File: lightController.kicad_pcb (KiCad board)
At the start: 2 copper layers, 91.4 x 87.6 mm, 66 parts, among them J1 VIN, J2 LED STRIP, J3 ICSP, J4 DEBUG, SW1 LIGHT_ON, SW2 SECT_0_ON, SW3 BRIGHT+, SW4 SECT_1_ON, SW5 BRIGHT-, SW6 SECT_2_ON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

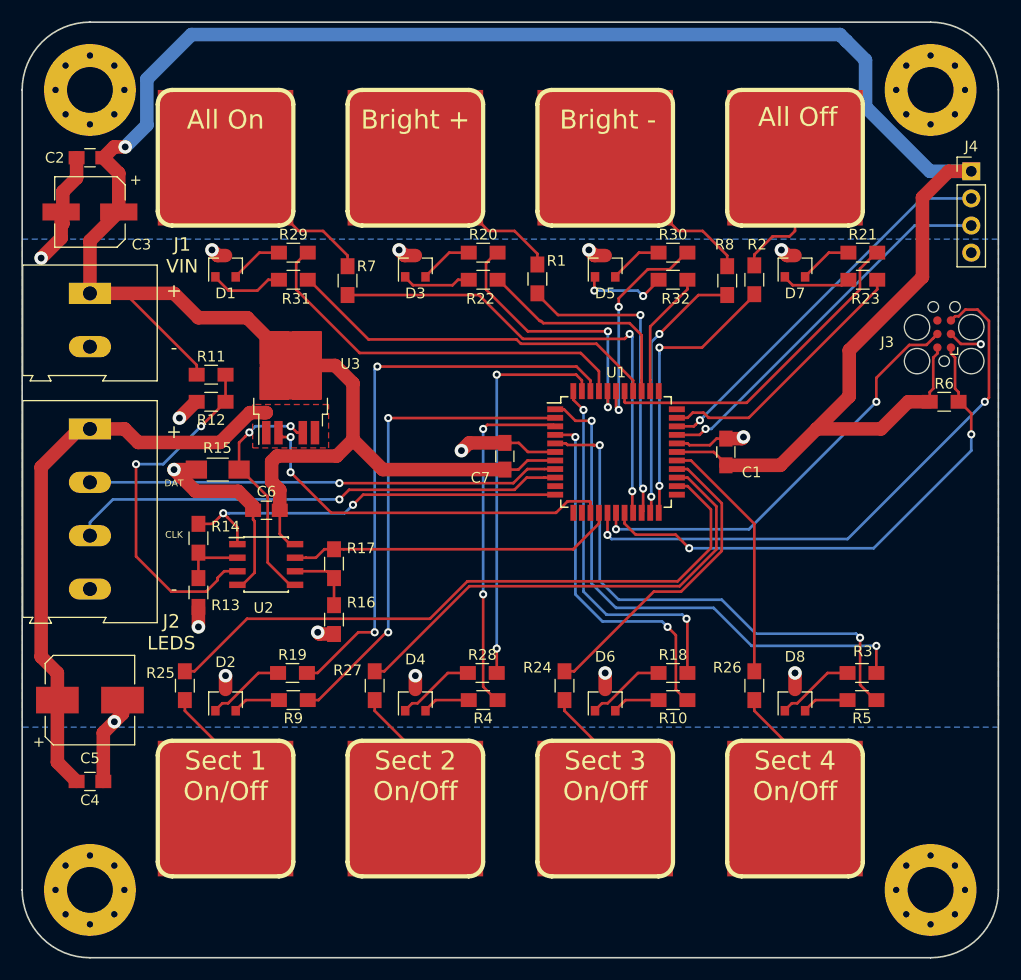
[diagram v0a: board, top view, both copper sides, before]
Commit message: Changed TX/RX to PORTB and I_SNS and PWR_EN accordingly Added SPI termination resistor footprints Added J5 GND pads
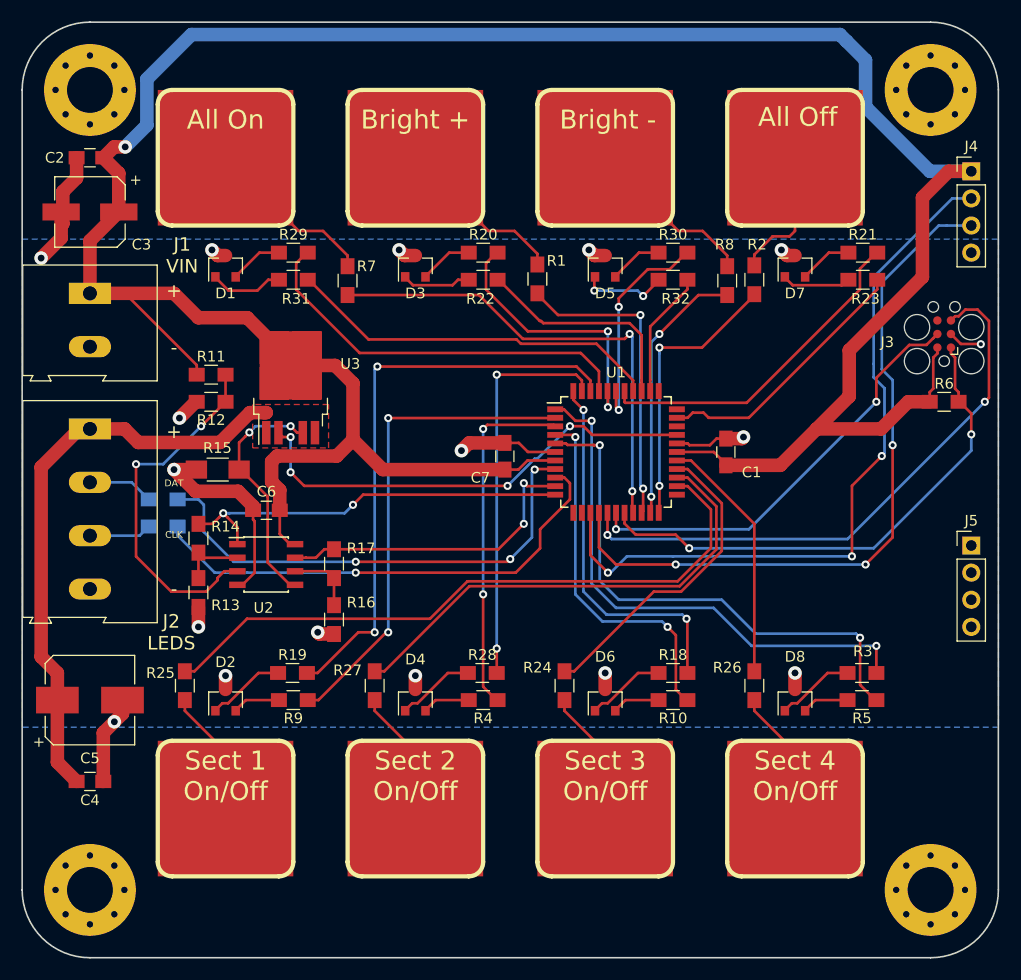
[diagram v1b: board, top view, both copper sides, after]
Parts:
- added J5: GND, Pin_Headers:Pin_Header_Straight_1x04_Pitch2.54mm, F.Cu at (174.0, 104.9)
- added R33: 1k, Resistors_SMD:R_0805_HandSoldering, B.Cu at (98.3, 103.1)
- added R34: 1k, Resistors_SMD:R_0805_HandSoldering, B.Cu at (98.3, 100.6)
- R15: value 1 -> 1k
- R17: value 4.99M -> 4.02k
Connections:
- H1 pad 1: (no net) -> Net-(H1-Pad1)
- H2 pad 1: (no net) -> Net-(H2-Pad1)
- H3 pad 1: (no net) -> Net-(H3-Pad1)
- H4 pad 1: (no net) -> Net-(H4-Pad1)
- J2 pad 2: /LED_DAT -> Net-(J2-Pad2)
- J2 pad 3: /LED_CLK -> Net-(J2-Pad3)
- J3 pad 6: (no net) -> Net-(J3-Pad6)
- U1 pad 10: (no net) -> /I_SNS
- U1 pad 12: (no net) -> Net-(U1-Pad12)
- U1 pad 13: (no net) -> Net-(U1-Pad13)
- U1 pad 14: /PWR_EN -> /DEBUG1
- U1 pad 15: /I_SNS -> /DEBUG2
- U1 pad 23: (no net) -> Net-(U1-Pad23)
- U1 pad 30: /DEBUG2 -> /PWR_EN
- U1 pad 31: /DEBUG1 -> Net-(U1-Pad31)
- U1 pad 33: (no net) -> Net-(U1-Pad33)
- U1 pad 34: (no net) -> Net-(U1-Pad34)
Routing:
- net /DEBUG1: track 36.4 -> 69.8 mm, vias 1 -> 3
- net /DEBUG2: track 35.7 -> 67.9 mm, vias 1 -> 3
- net /PWR_EN: track 35.7 -> 44.0 mm, vias 2 -> 4
- net Net-(J2-Pad2): track 0.00 -> 6.17 mm
- net Net-(J2-Pad3): track 0.00 -> 5.86 mm
- net /LED_DAT: track 44.2 -> 46.4 mm, vias 1 -> 3
- net /I_SNS: track 30.8 -> 29.6 mm, vias 0 -> 2
- net /LED_CLK: track 46.6 -> 46.0 mm
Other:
- board text added: "REV B1"
- board text removed: "REV A0"
